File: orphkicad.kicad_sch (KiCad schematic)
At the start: 41 parts, among them J1 USB_C_Receptacle_USB2.0_16P, J2 SWD, SW1 BTN_BOOT, SW2 BTN_RST, SW3 BTN_USR, U1 RP2040, U2 W25Q16JVUXIQ, U3 USBLC6-2SC6, U5 XC6206PxxxMR, X1 X322512MOB4SI 12pF

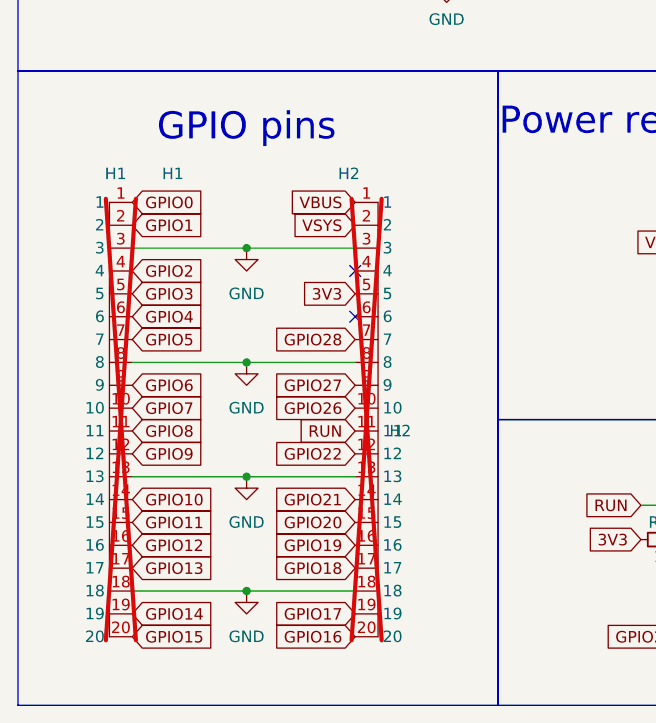
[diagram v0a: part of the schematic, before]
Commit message: Remove soldermask expansion on pin headers and fix false positive DRC errors
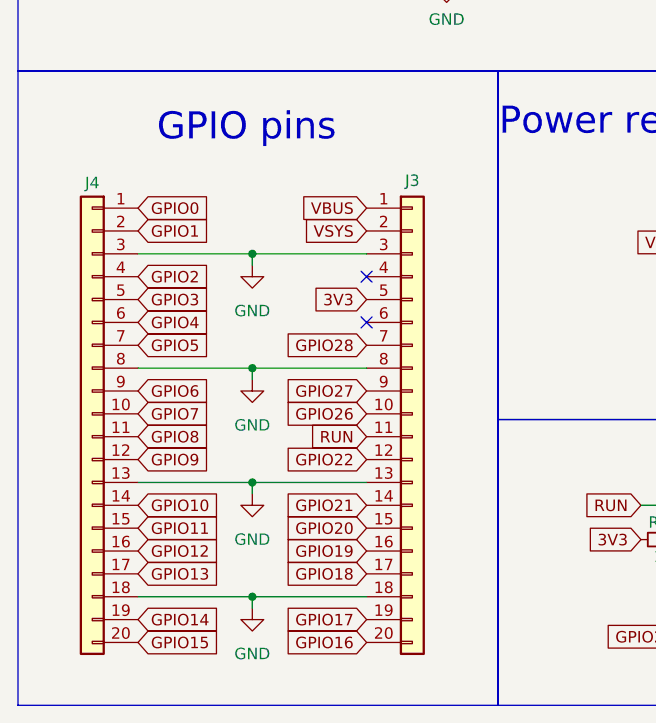
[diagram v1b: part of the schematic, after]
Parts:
- removed H1: H1, Headers:OrphPicoHeaders, symbol Headers:OrphPicoHeaders
- removed H2: H2, Headers:OrphPicoHeaders, symbol Headers:OrphPicoHeaders
- added J3, J4: Conn_01x20, Connector_PinSocket_2.54mm:PinSocket_1x20_P2.54mm_Vertical, symbol Connector_Generic:Conn_01x20
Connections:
- net 3V3: now also J3.5 (Pin_5)
- net GND: now also J3.13 (Pin_13), J3.18 (Pin_18), J3.3 (Pin_3), J3.8 (Pin_8), J4.13 (Pin_13), J4.18 (Pin_18), J4.3 (Pin_3), J4.8 (Pin_8)
- net GPIO0: now also J4.1 (Pin_1)
- net GPIO1: now also J4.2 (Pin_2)
- net GPIO10: now also J4.14 (Pin_14)
- net GPIO11: now also J4.15 (Pin_15)
- net GPIO12: now also J4.16 (Pin_16)
- net GPIO13: now also J4.17 (Pin_17)
- net GPIO14: now also J4.19 (Pin_19)
- net GPIO15: now also J4.20 (Pin_20)
- net GPIO16: now also J3.20 (Pin_20)
- net GPIO17: now also J3.19 (Pin_19)
- net GPIO18: now also J3.17 (Pin_17)
- net GPIO19: now also J3.16 (Pin_16)
- net GPIO2: now also J4.4 (Pin_4)
- net GPIO20: now also J3.15 (Pin_15)
- net GPIO21: now also J3.14 (Pin_14)
- net GPIO22: now also J3.12 (Pin_12)
- net GPIO26: now also J3.10 (Pin_10)
- net GPIO27: now also J3.9 (Pin_9)
- net GPIO28: now also J3.7 (Pin_7)
- net GPIO3: now also J4.5 (Pin_5)
- net GPIO4: now also J4.6 (Pin_6)
- net GPIO5: now also J4.7 (Pin_7)
- net GPIO6: now also J4.9 (Pin_9)
- net GPIO7: now also J4.10 (Pin_10)
- net GPIO8: now also J4.11 (Pin_11)
- net GPIO9: now also J4.12 (Pin_12)
- net RUN: now also J3.11 (Pin_11)
- net VBUS: now also J3.1 (Pin_1)
- net VSYS: now also J3.2 (Pin_2)

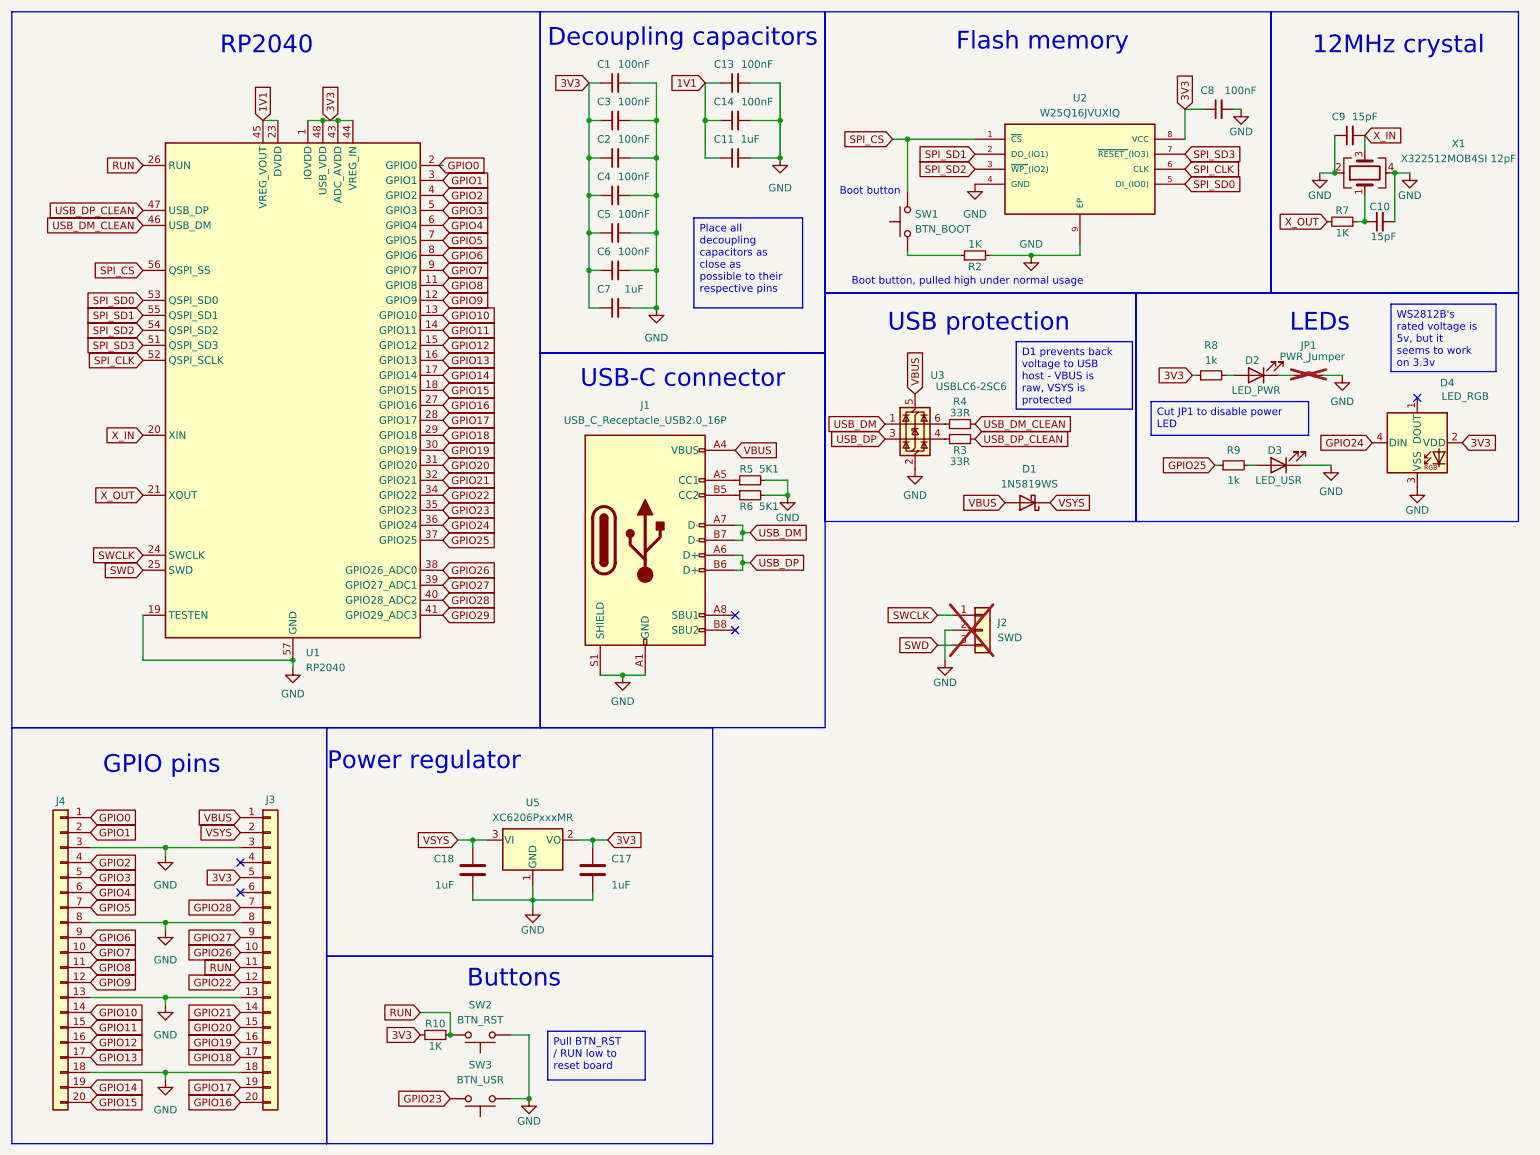
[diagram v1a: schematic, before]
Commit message: Pretty up schematic and make PCB footprints up-to-date
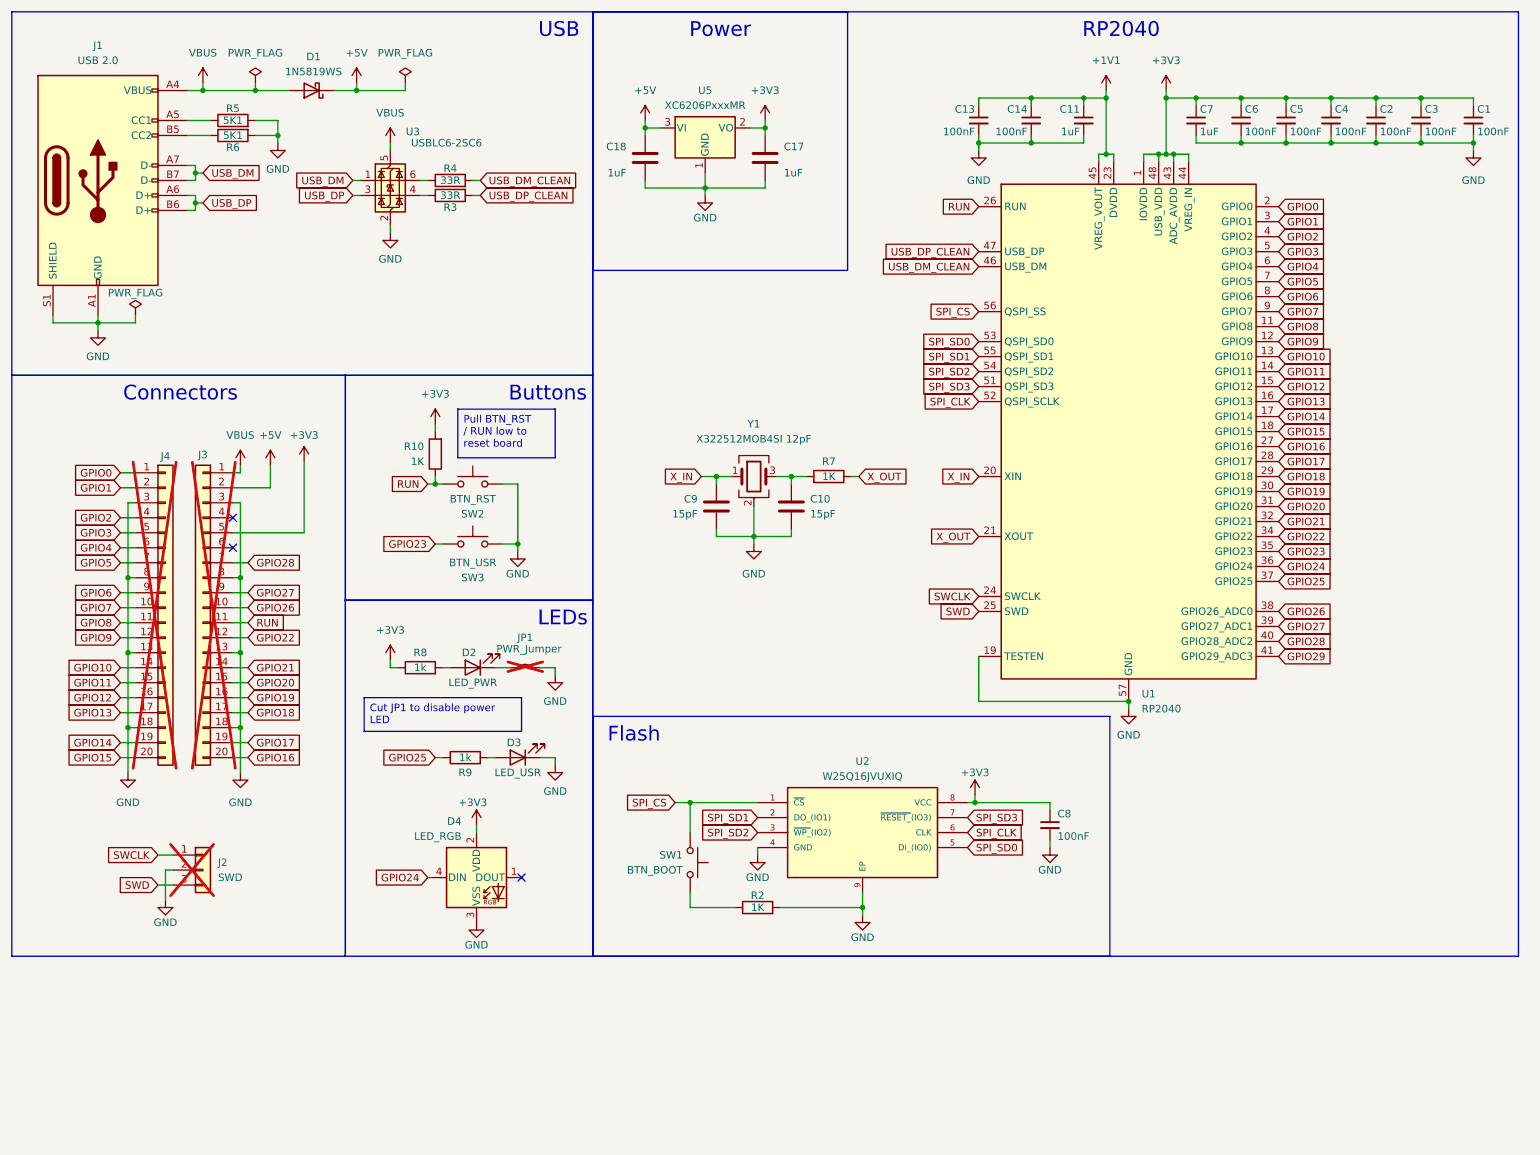
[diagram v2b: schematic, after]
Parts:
- removed J1: USB_C_Receptacle_USB2.0_16P, USBCConnectors:USB-C-SMD_TYPE-C-6PIN-2MD-073, symbol Connectors:TYPE-C_16PIN_2MD_073
- removed X1: X322512MOB4SI 12pF, Crystal:Crystal_SMD_3225-4Pin_3.2x2.5mm, symbol Crystals:X322512MSB4SI
- added J1: USB 2.0, USBCConnectors:USB-C-SMD_TYPE-C-6PIN-2MD-073, symbol Connector:USB_C_Receptacle_USB2.0_14P
- added Y1: X322512MOB4SI 12pF, Crystal:Crystal_SMD_3225-4Pin_3.2x2.5mm, symbol Device:Crystal_GND24
- C10, C9: symbol Device:C_Small -> Device:C
- J3, J4: now not fitted
- R10, R2, R3, R4, R5, R6, R7, R8, R9: symbol Device:R_Small -> Device:R
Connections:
- net GND: now also J1.A1 (GND), J1.A12 (GND), J1.B1 (GND), J1.B12 (GND), J1.S1 (SHIELD), Y1.2 (G), Y1.4 (G)
- net USB_DM: now also J1.A7 (D-), J1.B7 (D-)
- net USB_DP: now also J1.A6 (D+), J1.B6 (D+)
- net VBUS: now also J1.A4 (VBUS), J1.A9 (VBUS), J1.B4 (VBUS), J1.B9 (VBUS)
- net X_IN: now also Y1.1
- net X_OUT: now also R7.1; no longer R7.2
- net at C10.1: now also R7.2, Y1.3; no longer R7.1
- net at R6.1: now also J1.B5 (CC2)
- net at R5.1: now also J1.A5 (CC1)
- net 1V1 renamed +1V1
- net 3V3 renamed +3V3
- net VSYS renamed +5V
- no-connect marks 5 -> 3
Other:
- note added: "Connectors"
- note added: "Flash"
- note added: "Power"
- note added: "USB"
- note removed: "12MHz crystal"
- note removed: "Boot button"
- note removed: "Boot button, pulled high under normal usage"
- note removed: "Decoupling capacitors"
- note removed: "Flash memory"
- note removed: "GPIO pins"
- note removed: "Power regulator"
- note removed: "USB protection"
- note removed: "USB-C connector"
- moved on the sheet: C1, C10, C11, C13, C14, C17, C18, C2, C3, C4, C5, C6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

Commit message: seamless ordering :yay:
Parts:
- J1: FT Position Offset (none) -> 0,0.1905
- J3, J4: now left out of the parts list
- U1: FT Rotation Offset (none) -> -90
- U2: FT Rotation Offset (none) -> -90; HEIGHT 0.6mm -> (none); MANUFACTURER_NAME Winbond -> (none); MANUFACTURER_PART_NUMBER W25Q16JVUXIQ -> (none)

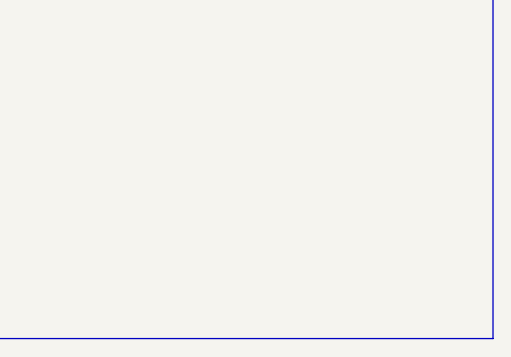
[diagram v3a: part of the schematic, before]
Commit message: Pinout site
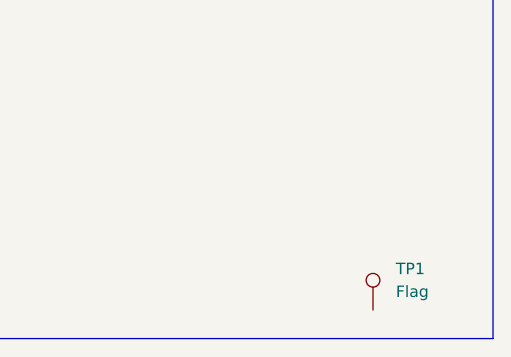
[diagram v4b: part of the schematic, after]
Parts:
- added TP1: Flag, orph-pico:flag, symbol Connector:TestPoint
